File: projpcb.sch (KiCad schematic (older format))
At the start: 25 parts, among them CON1 BARREL_JACK, CON2 BARREL_JACK, P1 CONN_01X02, P2 CONN_01X02, Q16 Q_NMOS_GSD, U1 Teensy_3.1, U2 LM358, U3 CD74HC4067, U4 CL520

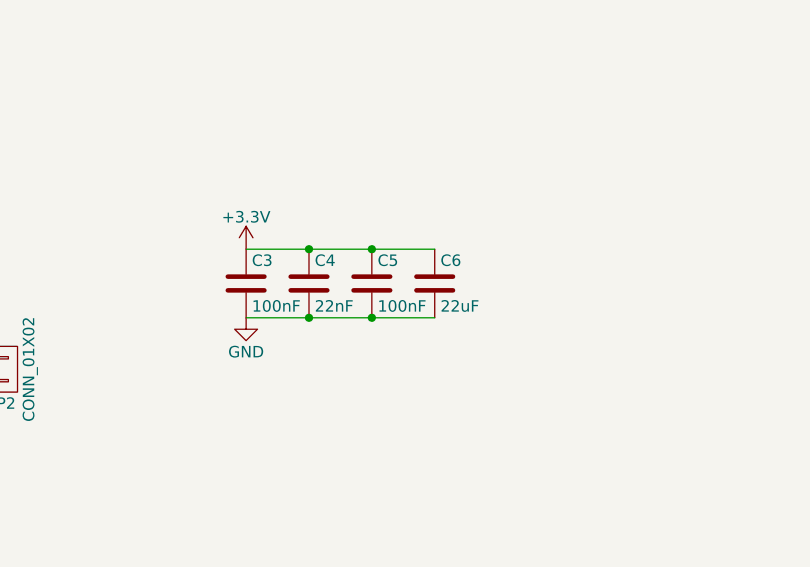
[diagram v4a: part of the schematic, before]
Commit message: More via stitching, more bypass for mux
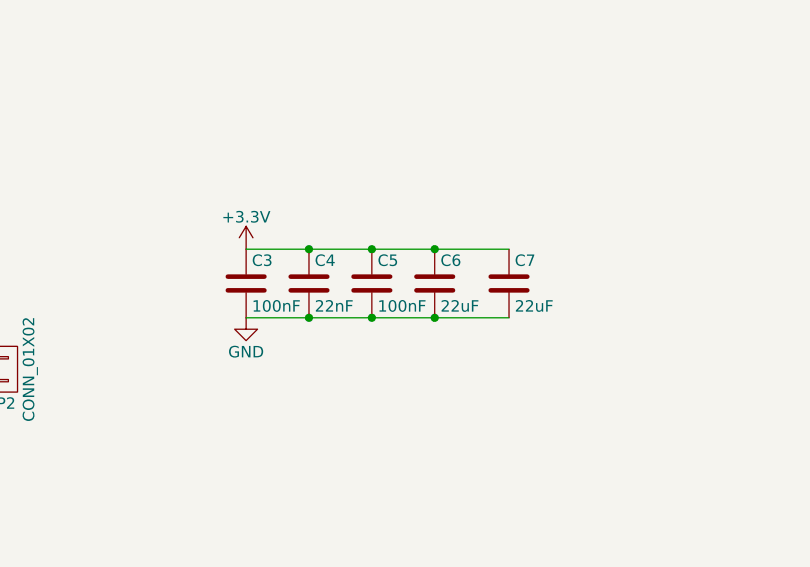
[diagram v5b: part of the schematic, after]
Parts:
- added C7: 22uF, Capacitors_SMD:C_0805_HandSoldering, symbol C
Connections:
- net +3V3: now also C7.1
- net GND: now also C7.2
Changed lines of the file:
@@
 LIBS:contrib
 LIBS:valves
-LIBS:teensy_3.1
-LIBS:sfh3711
-LIBS:cd74hc4067
-LIBS:cl520
 LIBS:projpcb-cache
 EELAYER 25 0
@@
 	5525 4350 5100 4350
 Wire Wire Line
-	8500 4800 9325 4800
+	8500 4800 9650 4800
 Connection ~ 8775 4800
 Wire Wire Line
-	8500 5100 9325 5100
+	8500 5100 9650 5100
 Connection ~ 8775 5100
 Connection ~ 9050 4800
@@
 	1275 4350 1200 4350
 $Comp
-L +3.3V #PWR011
+L +3.3V #PWR09
 U 1 1 56C856E8
 P 5350 1500
-F 0 "#PWR011" H 5350 1350 50  0001 C CNN
+F 0 "#PWR09" H 5350 1350 50  0001 C CNN
 F 1 "+3.3V" H 5350 1640 50  0000 C CNN
 F 2 "" H 5350 1500 50  0000 C CNN
@@
 Connection ~ 5350 1550
 $Comp
-L +3.3V #PWR012
+L +3.3V #PWR010
 U 1 1 56C86F91
 P 3025 1450
-F 0 "#PWR012" H 3025 1300 50  0001 C CNN
+F 0 "#PWR010" H 3025 1300 50  0001 C CNN
 F 1 "+3.3V" H 3025 1590 50  0000 C CNN
 F 2 "" H 3025 1450 50  0000 C CNN
@@
 $EndComp
 $Comp
-L +3.3V #PWR013
+L +3.3V #PWR011
 U 1 1 56C888B3
 P 4675 3350
-F 0 "#PWR013" H 4675 3200 50  0001 C CNN
+F 0 "#PWR011" H 4675 3200 50  0001 C CNN
 F 1 "+3.3V" H 4675 3490 50  0000 C CNN
 F 2 "" H 4675 3350 50  0000 C CNN
@@
 $EndComp
 $Comp
-L +3.3V #PWR014
+L +3.3V #PWR012
 U 1 1 56C89220
 P 6050 5275
-F 0 "#PWR014" H 6050 5125 50  0001 C CNN
+F 0 "#PWR012" H 6050 5125 50  0001 C CNN
 F 1 "+3.3V" H 6050 5415 50  0000 C CNN
 F 2 "" H 6050 5275 50  0000 C CNN
@@
 $EndComp
 $Comp
-L +3.3V #PWR015
+L +3.3V #PWR013
 U 1 1 56C892C4
 P 5150 5975
-F 0 "#PWR015" H 5150 5825 50  0001 C CNN
+F 0 "#PWR013" H 5150 5825 50  0001 C CNN
 F 1 "+3.3V" H 5150 6115 50  0000 C CNN
 F 2 "" H 5150 5975 50  0000 C CNN
@@
 $EndComp
 $Comp
-L GND #PWR016
+L GND #PWR014
 U 1 1 56C95CA8
 P 3150 3800
-F 0 "#PWR016" H 3150 3550 50  0001 C CNN
+F 0 "#PWR014" H 3150 3550 50  0001 C CNN
 F 1 "GND" H 3150 3650 50  0000 C CNN
 F 2 "" H 3150 3800 50  0000 C CNN
@@
 $EndComp
 $Comp
-L GND #PWR017
+L GND #PWR015
 U 1 1 56C95D5E
 P 3300 4075
-F 0 "#PWR017" H 3300 3825 50  0001 C CNN
+F 0 "#PWR015" H 3300 3825 50  0001 C CNN
 F 1 "GND" H 3300 3925 50  0000 C CNN
 F 2 "" H 3300 4075 50  0000 C CNN
@@
 $EndComp
 $Comp
-L GND #PWR018
+L GND #PWR016
 U 1 1 56C95E14
 P 3450 4350
-F 0 "#PWR018" H 3450 4100 50  0001 C CNN
+F 0 "#PWR016" H 3450 4100 50  0001 C CNN
 F 1 "GND" H 3450 4200 50  0000 C CNN
 F 2 "" H 3450 4350 50  0000 C CNN
@@
 	3450 2650 3025 2650
 $Comp
-L GND #PWR019
+L GND #PWR017
 U 1 1 56CD6885
 P 1025 1150
-F 0 "#PWR019" H 1025 900 50  0001 C CNN
+F 0 "#PWR017" H 1025 900 50  0001 C CNN
 F 1 "GND" H 1025 1000 50  0000 C CNN
 F 2 "" H 1025 1150 50  0000 C CNN
@@
 Connection ~ 5350 1850
 $Comp
-L GND #PWR020
+L GND #PWR018
 U 1 1 56E2450E
 P 4675 4350
-F 0 "#PWR020" H 4675 4100 50  0001 C CNN
+F 0 "#PWR018" H 4675 4100 50  0001 C CNN
 F 1 "GND" H 4675 4200 50  0000 C CNN
 F 2 "" H 4675 4350 50  0000 C CNN
@@
 $EndComp
 $Comp
-L GND #PWR021
+L GND #PWR019
 U 1 1 56E246E4
 P 5100 4350
-F 0 "#PWR021" H 5100 4100 50  0001 C CNN
+F 0 "#PWR019" H 5100 4100 50  0001 C CNN
 F 1 "GND" H 5100 4200 50  0000 C CNN
 F 2 "" H 5100 4350 50  0000 C CNN
@@
 $EndComp
 $Comp
-L GND #PWR022
+L GND #PWR020
 U 1 1 56E24872
 P 3150 1300
-F 0 "#PWR022" H 3150 1050 50  0001 C CNN
+F 0 "#PWR020" H 3150 1050 50  0001 C CNN
 F 1 "GND" H 3150 1150 50  0000 C CNN
 F 2 "" H 3150 1300 50  0000 C CNN
@@
 $EndComp
 $Comp
-L GND #PWR023
+L GND #PWR021
 U 1 1 56E24F5B
 P 3900 3425
-F 0 "#PWR023" H 3900 3175 50  0001 C CNN
+F 0 "#PWR021" H 3900 3175 50  0001 C CNN
 F 1 "GND" H 3900 3275 50  0000 C CNN
 F 2 "" H 3900 3425 50  0000 C CNN
@@
 $EndComp
 $Comp
-L GND #PWR024
+L GND #PWR022
 U 1 1 56E2557C
 P 5350 1875
-F 0 "#PWR024" H 5350 1625 50  0001 C CNN
+F 0 "#PWR022" H 5350 1625 50  0001 C CNN
 F 1 "GND" H 5350 1725 50  0000 C CNN
 F 2 "" H 5350 1875 50  0000 C CNN
@@
 $EndComp
 $Comp
-L GND #PWR028
+L GND #PWR023
 U 1 1 56E261BA
 P 5150 6375
-F 0 "#PWR028" H 5150 6125 50  0001 C CNN
+F 0 "#PWR023" H 5150 6125 50  0001 C CNN
 F 1 "GND" H 5150 6225 50  0000 C CNN
 F 2 "" H 5150 6375 50  0000 C CNN
@@
 	1    0    0    -1
 $EndComp
+$Comp
+L C C7
+U 1 1 578E0943
+P 9650 4950
+F 0 "C7" H 9675 5050 50  0000 L CNN
+F 1 "22uF" H 9675 4850 50  0000 L CNN
+F 2 "Capacitors_SMD:C_0805_HandSoldering" H 9688 4800 50  0001 C CNN
+F 3 "" H 9650 4950 50  0000 C CNN
+	1    9650 4950
+	1    0    0    -1
+$EndComp
+Connection ~ 9325 4800
+Connection ~ 9325 5100
 $EndSCHEMATC

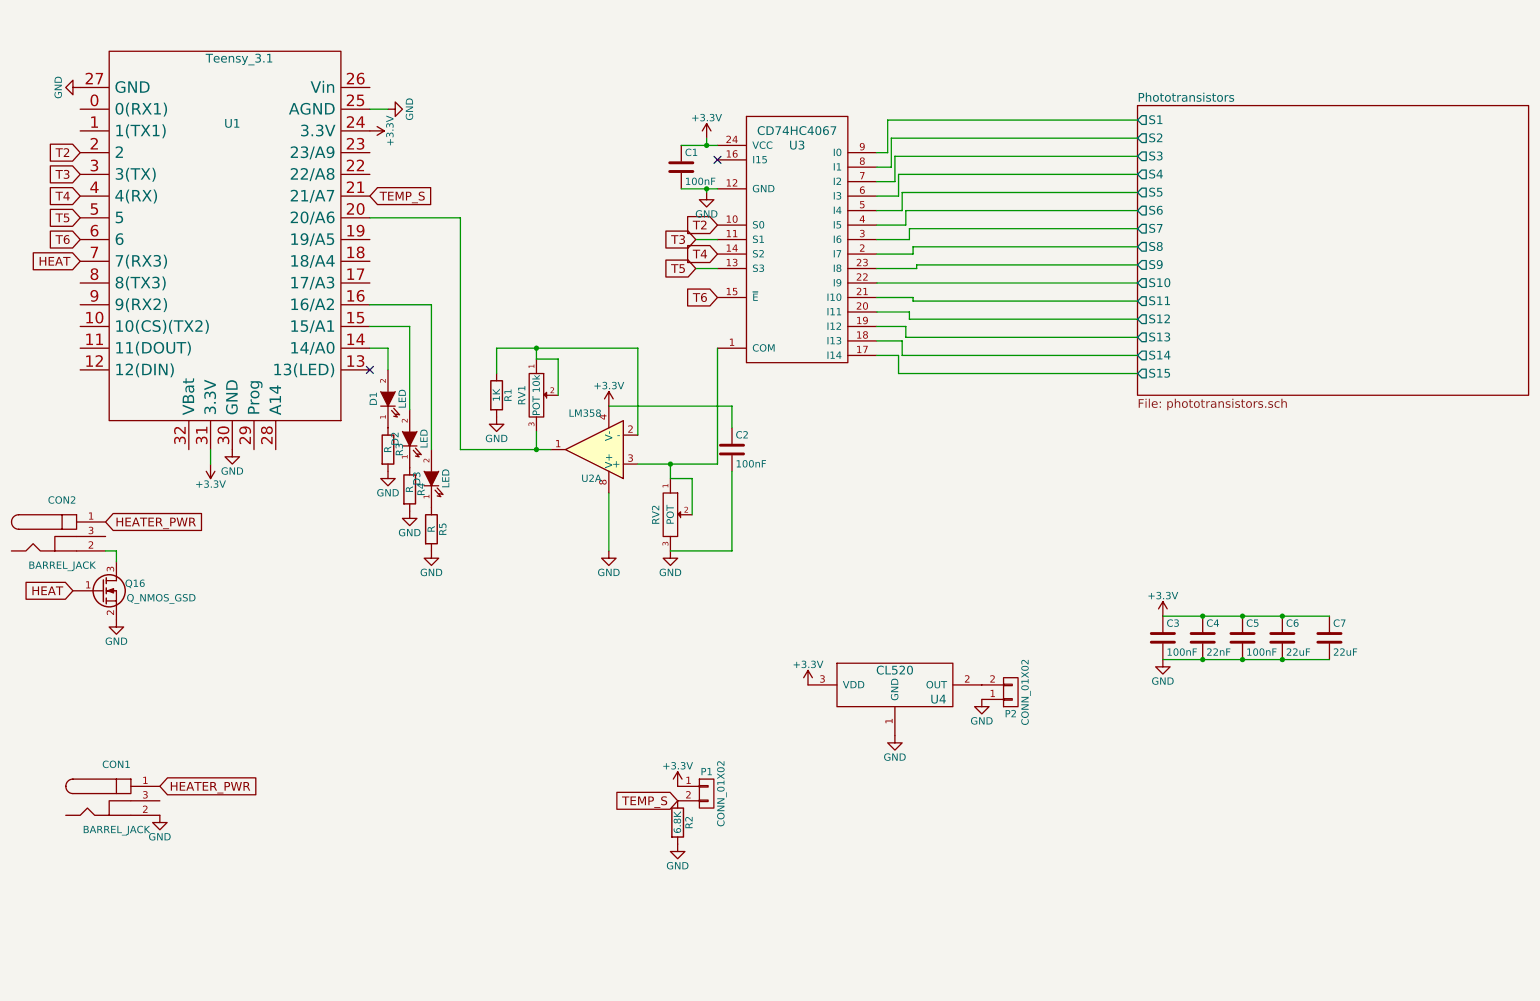
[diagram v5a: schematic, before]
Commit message: Big revamp
Added mosfet to LED output
Changed LED driver to NCR405U

Changed phototransistor array to be 9mm * 9mm to match standard 96 well
sizing

Added 5v Linear reg to feed the teensy as well as a jumper so we can do
initial tests using usb power
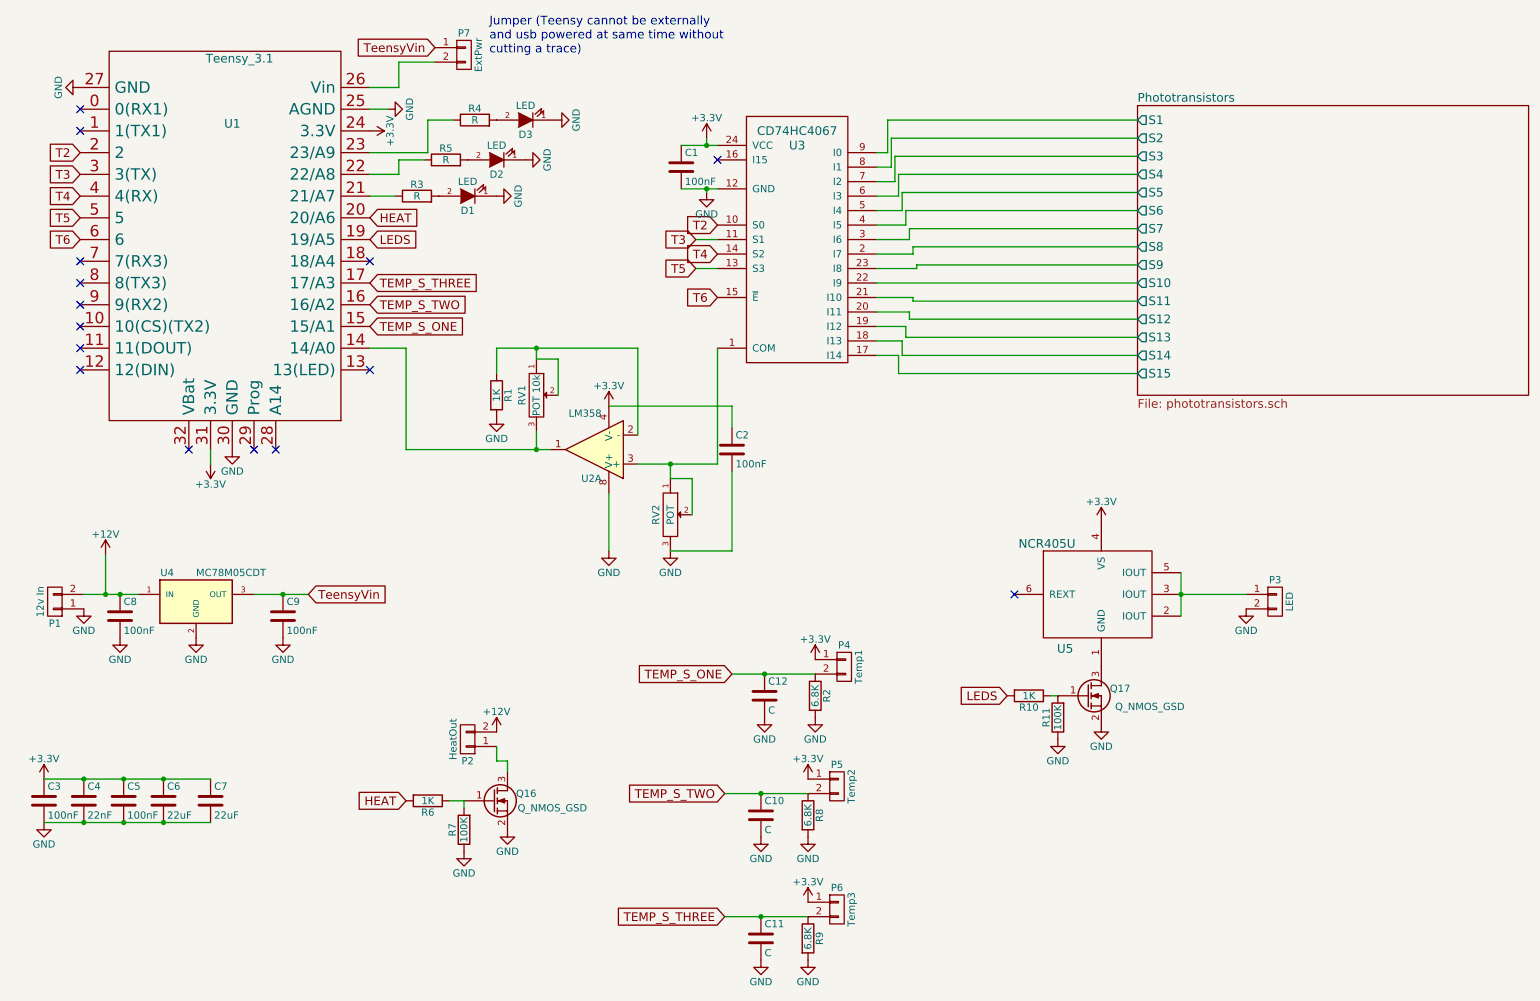
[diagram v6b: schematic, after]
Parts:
- removed CON1, CON2: BARREL_JACK, Connect:BARREL_JACK, symbol BARREL_JACK
- removed U4: CL520, TO_SOT_Packages_THT:TO-92_Inline_Narrow_Oval, symbol CL520
- added C10, C11, C12: C, Capacitors_SMD:C_0805_HandSoldering, symbol C
- added C8, C9: 100nF, Capacitors_SMD:C_0805_HandSoldering, symbol C
- added P1: 12v In, CustomConnect:2_5mm_screw_terminal, symbol CONN_01X02
- added P3: LED, CustomConnect:2_5mm_screw_terminal, symbol CONN_01X02
- added P5: Temp2, CustomConnect:2_5mm_screw_terminal, symbol CONN_01X02
- added P6: Temp3, CustomConnect:2_5mm_screw_terminal, symbol CONN_01X02
- added P7: ExtPwr, Pin_Headers:Pin_Header_Straight_1x02, symbol CONN_01X02
- added Q17: Q_NMOS_GSD, TO_SOT_Packages_SMD:SOT-23_Handsoldering, symbol Q_NMOS_GSD
- added R10, R6: 1K, Resistors_SMD:R_0805_HandSoldering, symbol R
- added R11, R7: 100K, Resistors_SMD:R_0805_HandSoldering, symbol R
- added R8, R9: 6.8K, Resistors_SMD:R_0805_HandSoldering, symbol R
- added U4: MC78M05CDT, TO_SOT_Packages_SMD:TO-252-2Lead, symbol MC78M05CDT
- added U5: NCR405U, modules:SOT457, symbol NCR405U
- P2: value CONN_01X02 -> HeatOut; footprint Pin_Headers:Pin_Header_Angled_1x02 -> CustomConnect:2_5mm_screw_terminal
- P4: renamed from P1; value CONN_01X02 -> Temp1; footprint Pin_Headers:Pin_Header_Straight_1x02 -> CustomConnect:2_5mm_screw_terminal
- renumbered D3 to D2, D2 to D3
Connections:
- net +3V3: now also P5.1 (P1), P6.1 (P1), U5.4 (VS)
- net GND: now also D1.1 (K), D2.1 (K), D3.1 (K), C10.2, C11.2, C12.2, C8.2, C9.2, P1.1 (P1), P3.2 (P2), Q17.2 (S), R11.1, R7.1, R8.2, R9.2, U4.2 (GND); no longer P2.1 (P1), R3.2, R4.2, R5.2
- net HEAT: now also U1.20 (20/A6), R6.2; no longer Q16.1 (G), U1.7 (7(RX3))
- net at U1.14 (14/A0): now also RV1.3, U2.1; no longer D1.2 (A)
- net at D3.2 (A): now also R4.2; no longer U1.15 (15/A1)
- net at D2.2 (A): now also R5.2; no longer U1.16 (16/A2)
- net TEMP_S_THREE: now reaches U1.17 (17/A3)
- net TEMP_S_THREE: now also C11.1, P6.2 (P2), R9.1
- net LEDS: now reaches U1.19 (19/A5)
- net LEDS: now also R10.2
- net at U1.22 (22/A8): now also R5.1
- net at U1.23 (23/A9): now also R4.1
- net at U1.26 (Vin): now also P7.2 (P2)
- net at Q16.3 (D): now also P2.1 (P1)
- net +12V: now reaches P2.2 (P2)
- net +12V: now also C8.1, P1.2 (P2), U4.1 (IN)
- net at R3.1: now also U1.21 (21/A7); no longer D1.1 (K)
- net TEMP_S renamed TEMP_S_ONE
- net TEMP_S_ONE: now also U1.15 (15/A1), C12.1; no longer U1.21 (21/A7)
- new net: Q16.1 (G), R6.1, R7.2
- new net: D1.2 (A), R3.2
- new net: Q17.3 (D), U5.1 (GND)
- new net: P3.1 (P1), U5.2 (IOUT), U5.3 (IOUT), U5.5 (IOUT)
- new net: Q17.1 (G), R10.1, R11.2
- new net TEMP_S_TWO: C10.1, P5.2 (P2), R8.1, U1.16 (16/A2)
- new net TeensyVin: C9.1, P7.1 (P1), U4.3 (OUT)
- no-connect marks 2 -> 15
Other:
- note added: "Jumper (Teensy cannot be externally\nand usb powered at same time without\ncutting a trace)"
- moved on the sheet: C3, C4, C5, C6, C7, D1, D2, D3, P4, Q16, R2, R3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
